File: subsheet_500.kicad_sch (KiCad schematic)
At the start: 27 parts, among them J500 DM-15S — JOY0, J501 DM-15S — JOY1, U513 LM556_DUAL_TIMER_PHY, U514 LM556_DUAL_TIMER_PHY

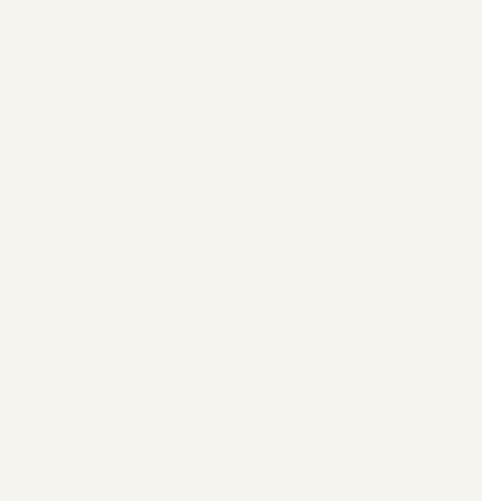
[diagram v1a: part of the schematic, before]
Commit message: add gnd/vcc symbol to start replacing local labels
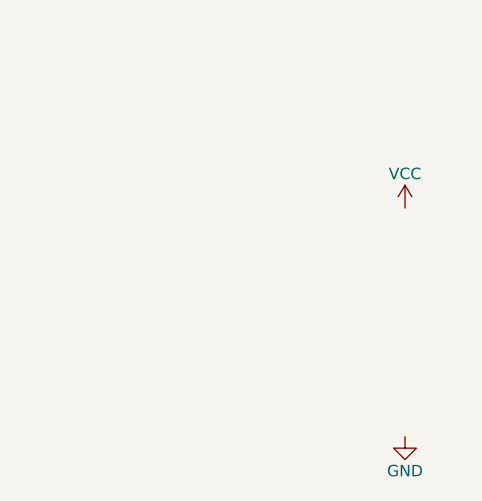
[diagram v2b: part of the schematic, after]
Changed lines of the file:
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@@
     (pin "2")
   )
+  (symbol (lib_id "power:VCC") (at 187.96 214.63 0) (unit 1)
+    (in_bom yes) (on_board yes)
+    (property "Reference" "#PWR?" (id 0) (at 187.96 218.44 0)
+      (effects (font (size 1.27 1.27)) hide)
+    )
+    (property "Value" "VCC" (id 1) (at 187.96 210.82 0))
+    (property "Footprint" "" (id 2) (at 187.96 214.63 0)
+      (effects (font (size 1.27 1.27)) hide)
+    )
+    (property "Datasheet" "" (id 3) (at 187.96 214.63 0)
+      (effects (font (size 1.27 1.27)) hide)
+    )
+    (pin "1")
+  )
+  (symbol (lib_id "power:GND") (at 187.96 240.03 0) (unit 1)
+    (in_bom yes) (on_board yes)
+    (property "Reference" "#PWR?" (id 0) (at 187.96 246.38 0)
+      (effects (font (size 1.27 1.27)) hide)
+    )
+    (property "Value" "GND" (id 1) (at 187.96 243.84 0))
+    (property "Footprint" "" (id 2) (at 187.96 240.03 0)
+      (effects (font (size 1.27 1.27)) hide)
+    )
+    (property "Datasheet" "" (id 3) (at 187.96 240.03 0)
+      (effects (font (size 1.27 1.27)) hide)
+    )
+    (pin "1")
+  )
 )
